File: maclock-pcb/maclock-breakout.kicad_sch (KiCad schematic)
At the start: 10 parts, among them SW1 SW_Push, SW2 SW_Push

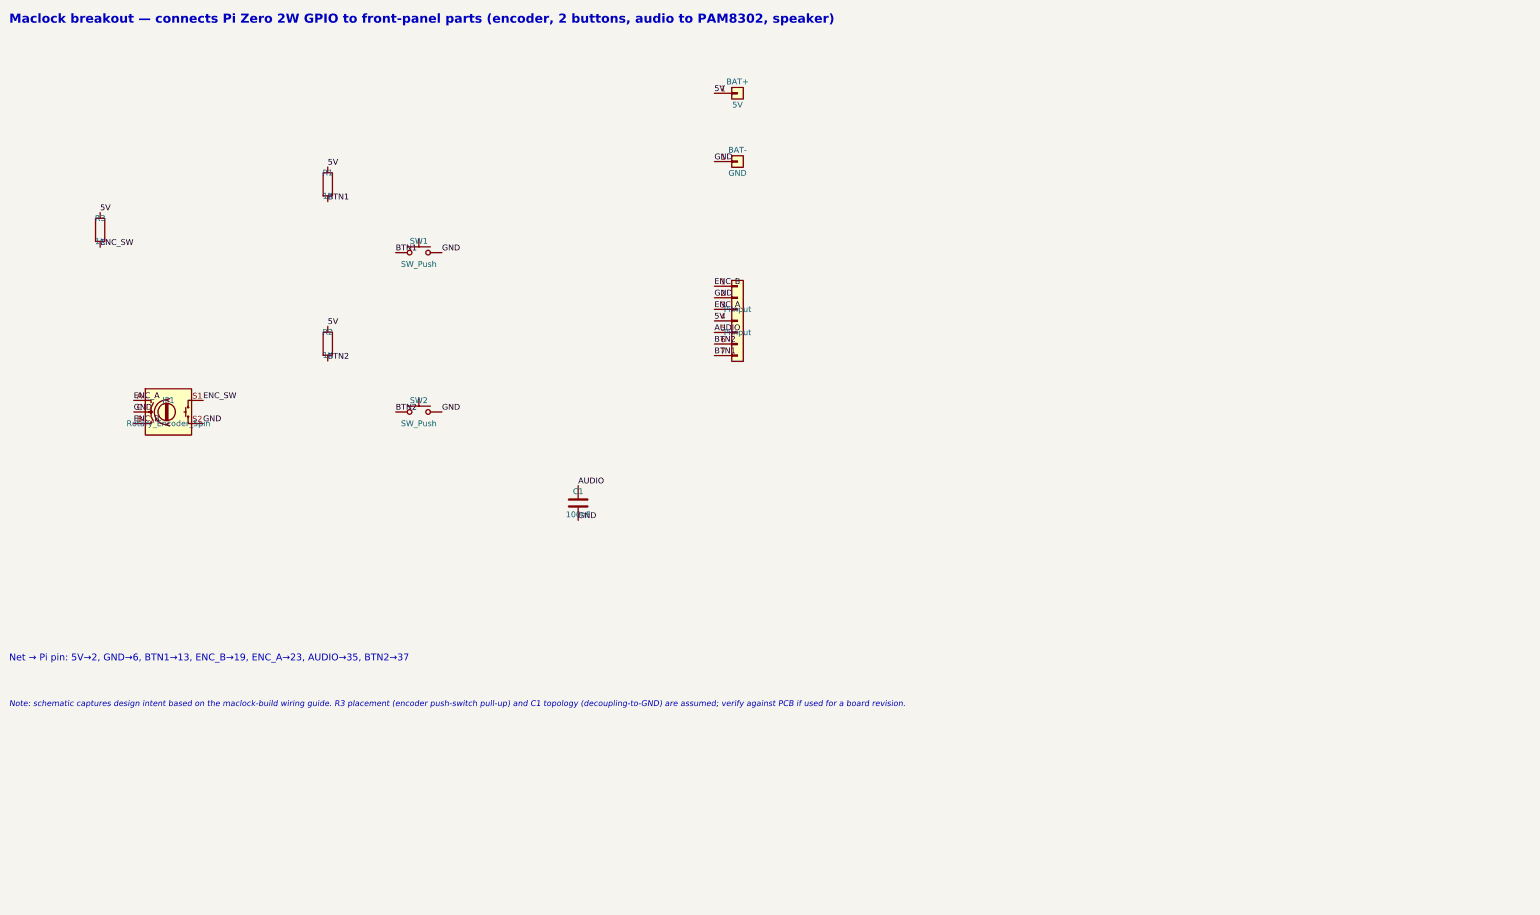
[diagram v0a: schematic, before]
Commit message: PCB: real HYCW03 encoder, LCSC-sourceable BOM, rebuilt schematic
- ENC1: F-Switch E8E8-3.2C60-9B34 (not on LCSC) -> HOAUC HYCW03-2.8D-5P-S
  (C55218995); new footprint, bore placed 8.8mm from the left edge / 4mm from
  the bottom to keep the dial aligned with the case
- Nets: split the series-resistor button nets (BTN1/SW1, BTN2/SW2) so each is
  fully connected; assigned ENC1 pad nets; normalized all board nets to the
  /-prefixed hierarchical form to match the schematic
- Rebuilt maclock-breakout.kicad_sch from the PCB (was a PiInput-only stub):
  all 11 parts with correct footprints/values/LCSC, custom ENC1 symbol in
  maclock.kicad_sym; ERC 0/0, board<->schematic parity clean but for benign
  symbol metadata
- BOM: every part now resolves to an LCSC number (added J1 C158011, J2 C157997);
  PCBWAY_REPLY.md answers the quote's four flagged parts
- Switches: added TS24CA and TSB001 side-switch footprints as LCSC-stocked
  alternatives to the Same Sky TS32; board left on the TS32 for hand-positioning
- scripts/: reproducible pcbnew edits (bundled Python) for each board change
- README: BOM, sourcing, J1 power switch / J2 power input, schematic status
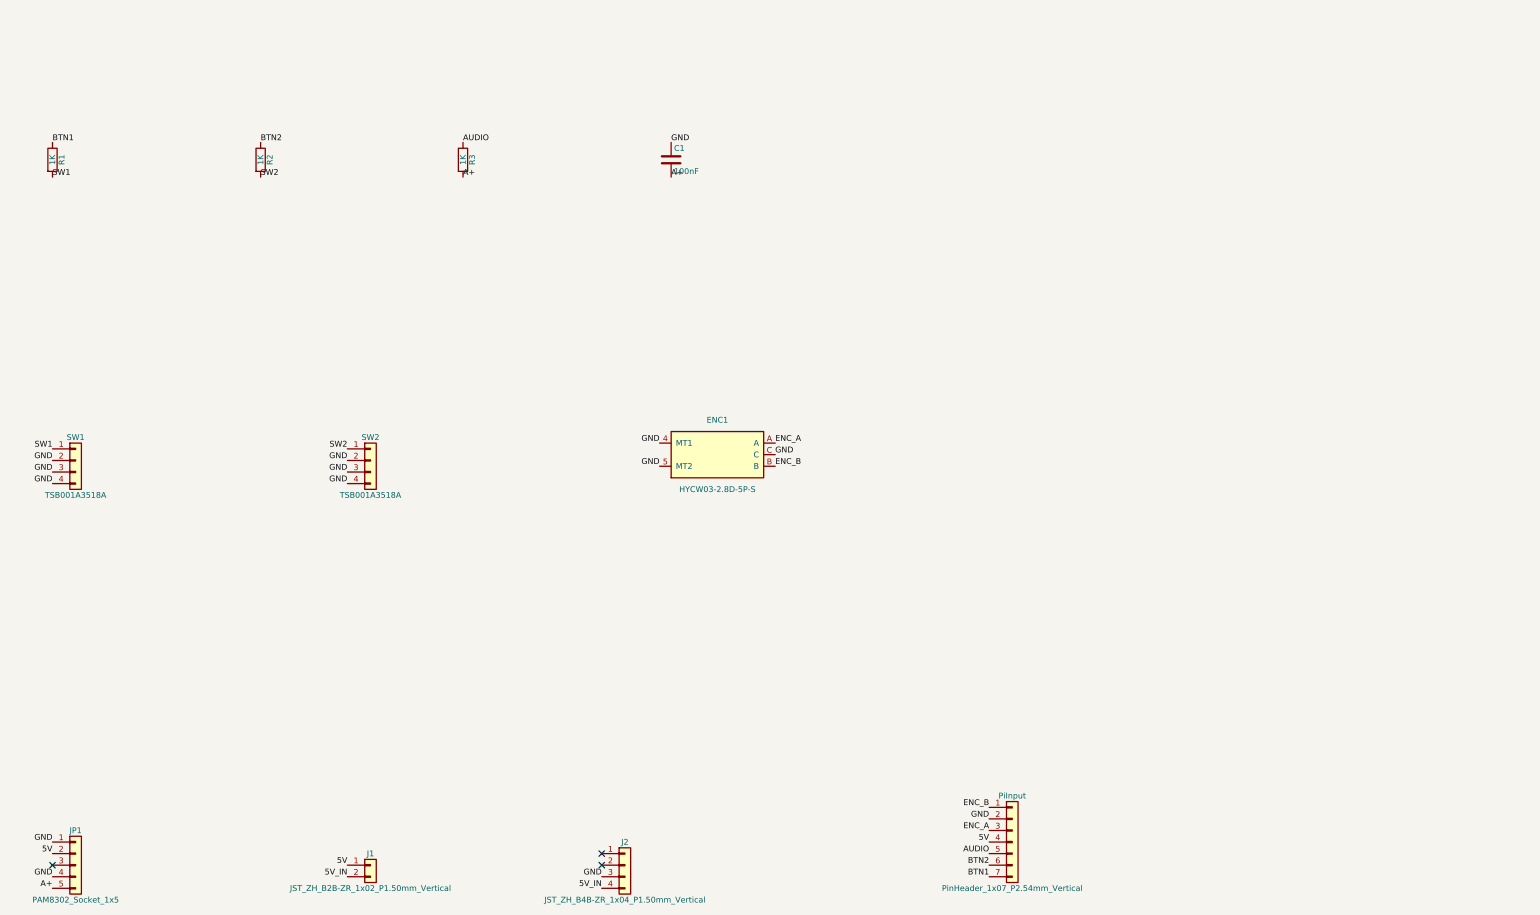
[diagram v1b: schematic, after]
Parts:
- removed BAT+: 5V, symbol Connector_Generic:Conn_01x01
- removed BAT-: GND, symbol Connector_Generic:Conn_01x01
- removed JP1: Rotary_Encoder_5pin, KiCad:1X05_ROUND_70, symbol Device:RotaryEncoder_Switch
- removed SW1, SW2: SW_Push, KiCad:TS32735BK160RASMTTR, symbol Switch:SW_Push
- added ENC1: HYCW03-2.8D-5P-S, maclock:RotaryEncoder_HYCW03-2.8D-5P-S_SMD, symbol maclock:RotaryEncoder_HYCW03-2.8D-5P-S
- added J1: JST_ZH_B2B-ZR_1x02_P1.50mm_Vertical, Connector_JST:JST_ZH_B2B-ZR_1x02_P1.50mm_Vertical, symbol Connector_Generic:Conn_01x02
- added J2: JST_ZH_B4B-ZR_1x04_P1.50mm_Vertical, Connector_JST:JST_ZH_B4B-ZR_1x04_P1.50mm_Vertical, symbol Connector_Generic:Conn_01x04
- added JP1: PAM8302_Socket_1x5, Connector_PinSocket_2.54mm:PinSocket_1x05_P2.54mm_Vertical, symbol Connector_Generic:Conn_01x05
- added SW1, SW2: TSB001A3518A, maclock:SW_TSB001_7.7x3.55_SideSMD, symbol Connector_Generic:Conn_01x04
- C1: footprint Capacitor_THT:C_Disc_D6.0mm_W2.5mm_P5.00mm -> maclock:C_Chip_or_Disc_P5mm_SMD; LCSC (none) -> C24497
- PiInput: value PiInput -> PinHeader_1x07_P2.54mm_Vertical; LCSC (none) -> C492406
- R1, R2, R3: LCSC (none) -> C11702
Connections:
- net 5V: now also J1.1 (Pin_1), JP1.2 (Pin_2); no longer R1.1, R2.1, R3.1
- net AUDIO: now also R3.1; no longer C1.1
- net BTN1: now also R1.1; no longer R1.2
- net BTN2: now also R2.1; no longer R2.2
- net ENC_A: now also ENC1.A
- net ENC_B: now also ENC1.B
- net GND: now also C1.1, ENC1.4 (MT1), ENC1.5 (MT2), ENC1.C, J2.3 (Pin_3), JP1.1 (Pin_1), JP1.4 (Pin_4), SW1.2 (Pin_2), SW1.3 (Pin_3), SW1.4 (Pin_4), SW2.2 (Pin_2), SW2.3 (Pin_3), SW2.4 (Pin_4); no longer C1.2
- net ENC_SW renamed A+
- net A+: now also C1.2, JP1.5 (Pin_5)
- new net 5V_IN: J1.2 (Pin_2), J2.4 (Pin_4)
- new net SW1: R1.2, SW1.1 (Pin_1)
- new net SW2: R2.2, SW2.1 (Pin_1)
- no-connect marks 0 -> 3
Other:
- note removed: "Maclock breakout — connects Pi Zero 2W GPIO to front-panel parts (encoder, 2 buttons, audio to PAM8302, speaker)"
- note removed: "Net → Pi pin: 5V→2, GND→6, BTN1→13, ENC_B→19, ENC_A→23, AUDIO→35, BTN2→37"
- note removed: "Note: schematic captures design intent based on the maclock-build wiring guide. R3 placement (encoder push-switch pull-up) and C1 topology (decoupling-to-GND) are assumed; verify against PCB if used for a board revision."

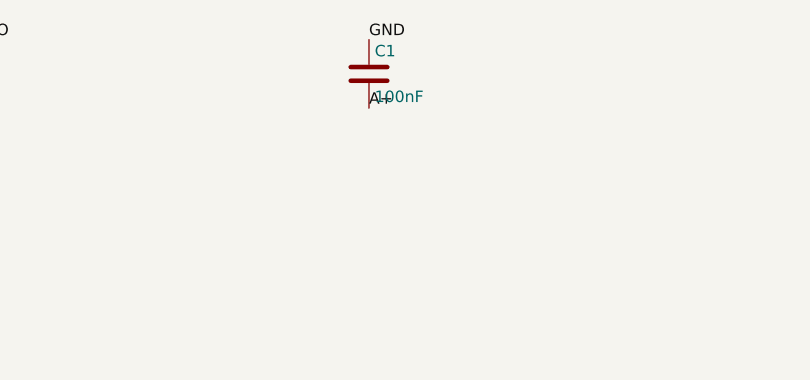
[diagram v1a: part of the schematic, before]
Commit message: PCB: TSB001 part numbers on board, C1 10nF audio LPF, J2 polarity silk, project lib tables, C1 1206 model
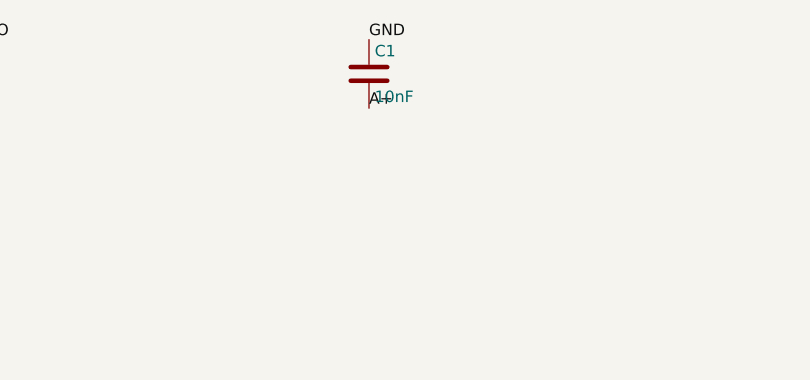
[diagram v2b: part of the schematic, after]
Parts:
- C1: value 100nF -> 10nF; LCSC C24497 -> C1846
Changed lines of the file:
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@@
 			)
 		)
-		(property "Value" "100nF"
+		(property "Value" "10nF"
 			(at 186.055 57.15 0)
 			(effects
@@
 			)
 		)
-		(property "LCSC" "C24497"
+		(property "LCSC" "C1846"
 			(at 185.42 54.61 0)
 			(hide yes)

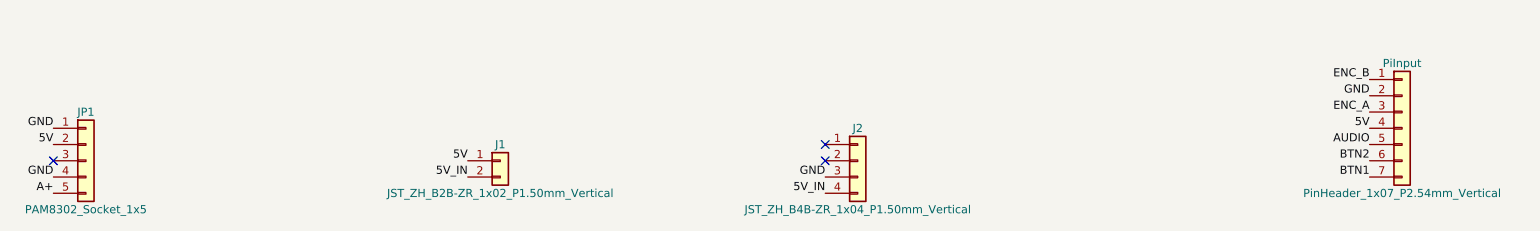
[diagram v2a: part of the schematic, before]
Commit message: PCB: connector MPN values, 1.0 mm 5V supply tracks
- J1/J2/JP1/PiInput Value -> B2B-ZR(LF)(SN) / B4B-ZR(LF)(SN) / 2.54-1*5PFemale / PZ254V-11-07P
  on board and schematic (PCBway reads the board's Value column)
- /5V and /5V_IN tracks 0.5 -> 1.0 mm; the J2 pad-1 skirt is 0.8 mm and the diagonal out of
  JP1 pin 2 stays 0.5 mm (2.54 mm socket pitch); long y=98 run restarted at x=141 with a stub
  so its round end clears JP1 pin 1 (GND)
- DRC 0 errors / 0 unconnected; ERC 0; scripts/mpn_values_and_wide_5v.py
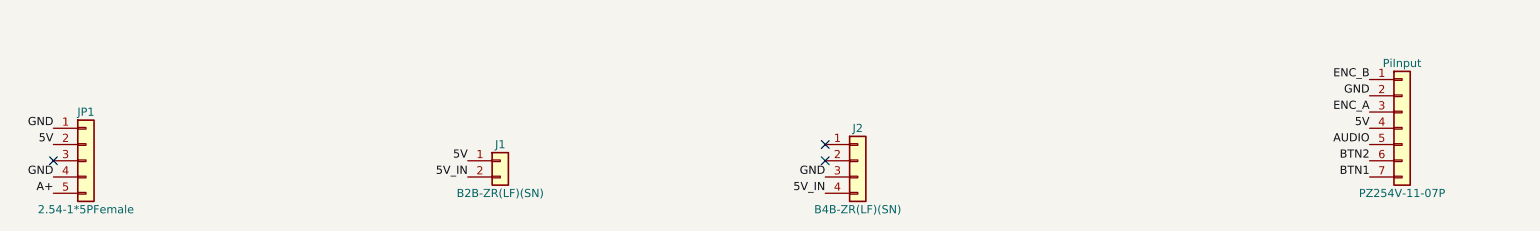
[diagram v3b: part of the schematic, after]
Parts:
- J1: value JST_ZH_B2B-ZR_1x02_P1.50mm_Vertical -> B2B-ZR(LF)(SN)
- J2: value JST_ZH_B4B-ZR_1x04_P1.50mm_Vertical -> B4B-ZR(LF)(SN)
- JP1: value PAM8302_Socket_1x5 -> 2.54-1*5PFemale
- PiInput: value PinHeader_1x07_P2.54mm_Vertical -> PZ254V-11-07P
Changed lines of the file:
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@@
 			)
 		)
-		(property "Value" "PAM8302_Socket_1x5"
+		(property "Value" "2.54-1*5PFemale"
 			(at 54.61 217.17 0)
 			(effects
@@
 			)
 		)
-		(property "Value" "JST_ZH_B2B-ZR_1x02_P1.50mm_Vertical"
+		(property "Value" "B2B-ZR(LF)(SN)"
 			(at 119.38 214.63 0)
 			(effects
@@
 			)
 		)
-		(property "Value" "JST_ZH_B4B-ZR_1x04_P1.50mm_Vertical"
+		(property "Value" "B4B-ZR(LF)(SN)"
 			(at 175.26 217.17 0)
 			(effects
@@
 			)
 		)
-		(property "Value" "PinHeader_1x07_P2.54mm_Vertical"
+		(property "Value" "PZ254V-11-07P"
 			(at 260.35 214.63 0)
 			(effects

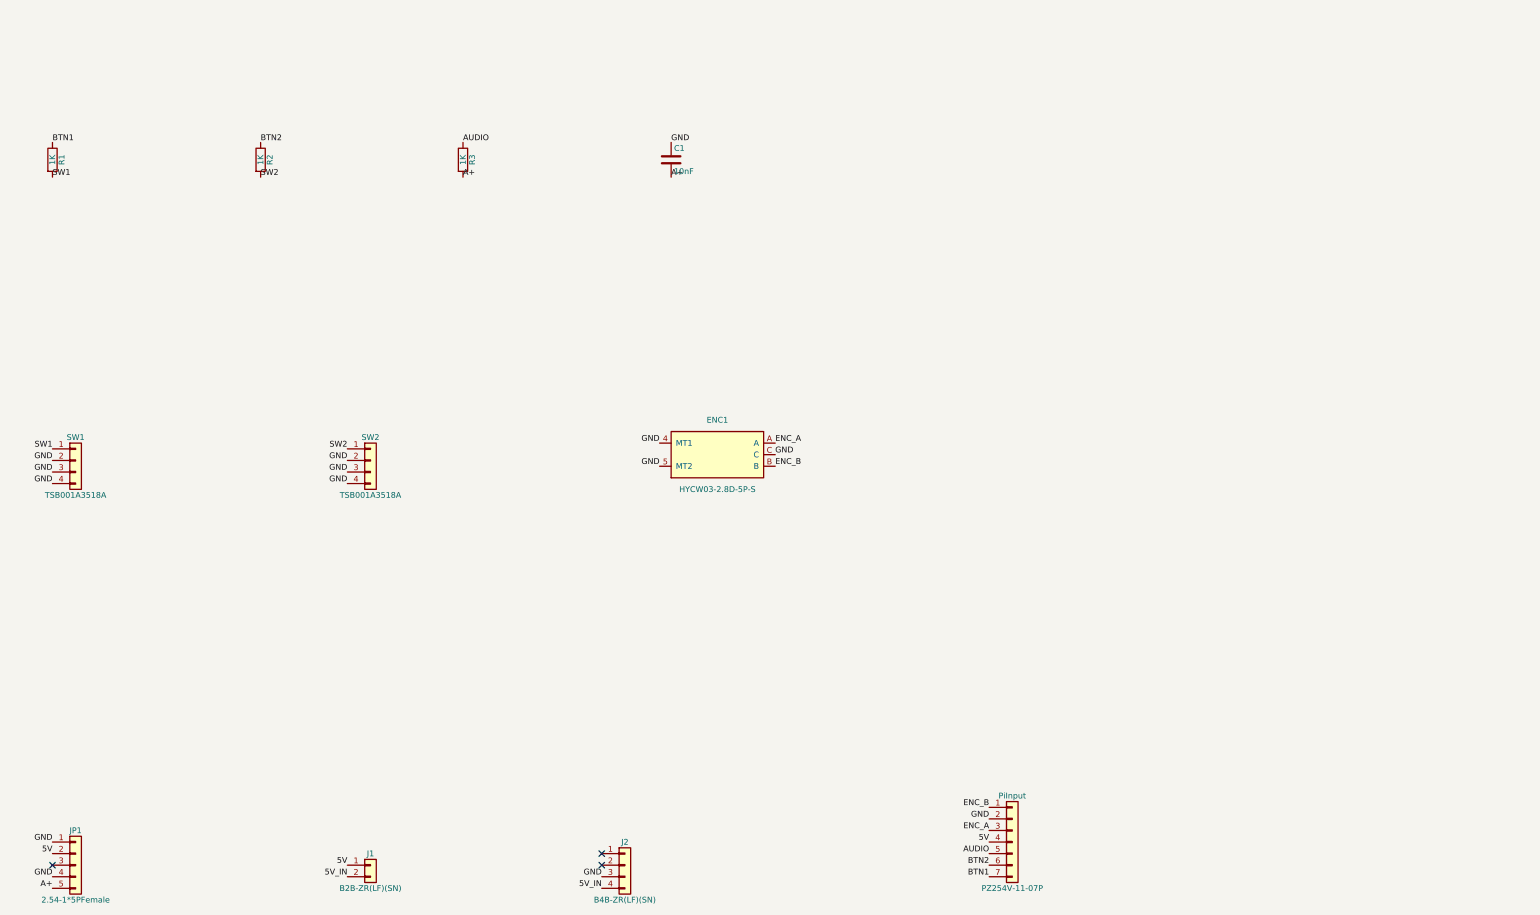
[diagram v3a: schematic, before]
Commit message: PCB rev 2: on-board PAM8302A amp replaces the Adafruit module
- U1 PAM8302AASCR (C113367) on the bottom side where the JP1 socket was; JP1 removed
- Input: A+ -> C2 220n -> R4 47k -> IN+; IN- via R5 47k + C3 220n to GND (gain ~9 dB)
- C4 1u + C5 10u decoupling, fed by via from the F.Cu 5V trunk; new 5V via at the old
  JP1 pin-2 spot keeps the F.Cu/B.Cu 5V runs joined
- SD pulled up by R6 100k; also brought out on a new PiInput pin 8 (MUTE) along the
  top edge, so the header is now 1x8 (C492407)
- J3 JST ZH 2P speaker connector (C158011), + / - silk, pad 1 = SPK+
- Schematic: new parts + nets, PWR_FLAGs on 5V/GND; ERC 0/0. DRC 0 errors, 0 unconnected,
  parity only benign field/NC notes. scripts/add_onboard_amp.py rebuilds it from 5ece6d9
- Docs: PCB README BOM + amp section, PCBway reply, build-guide wiring table, root README
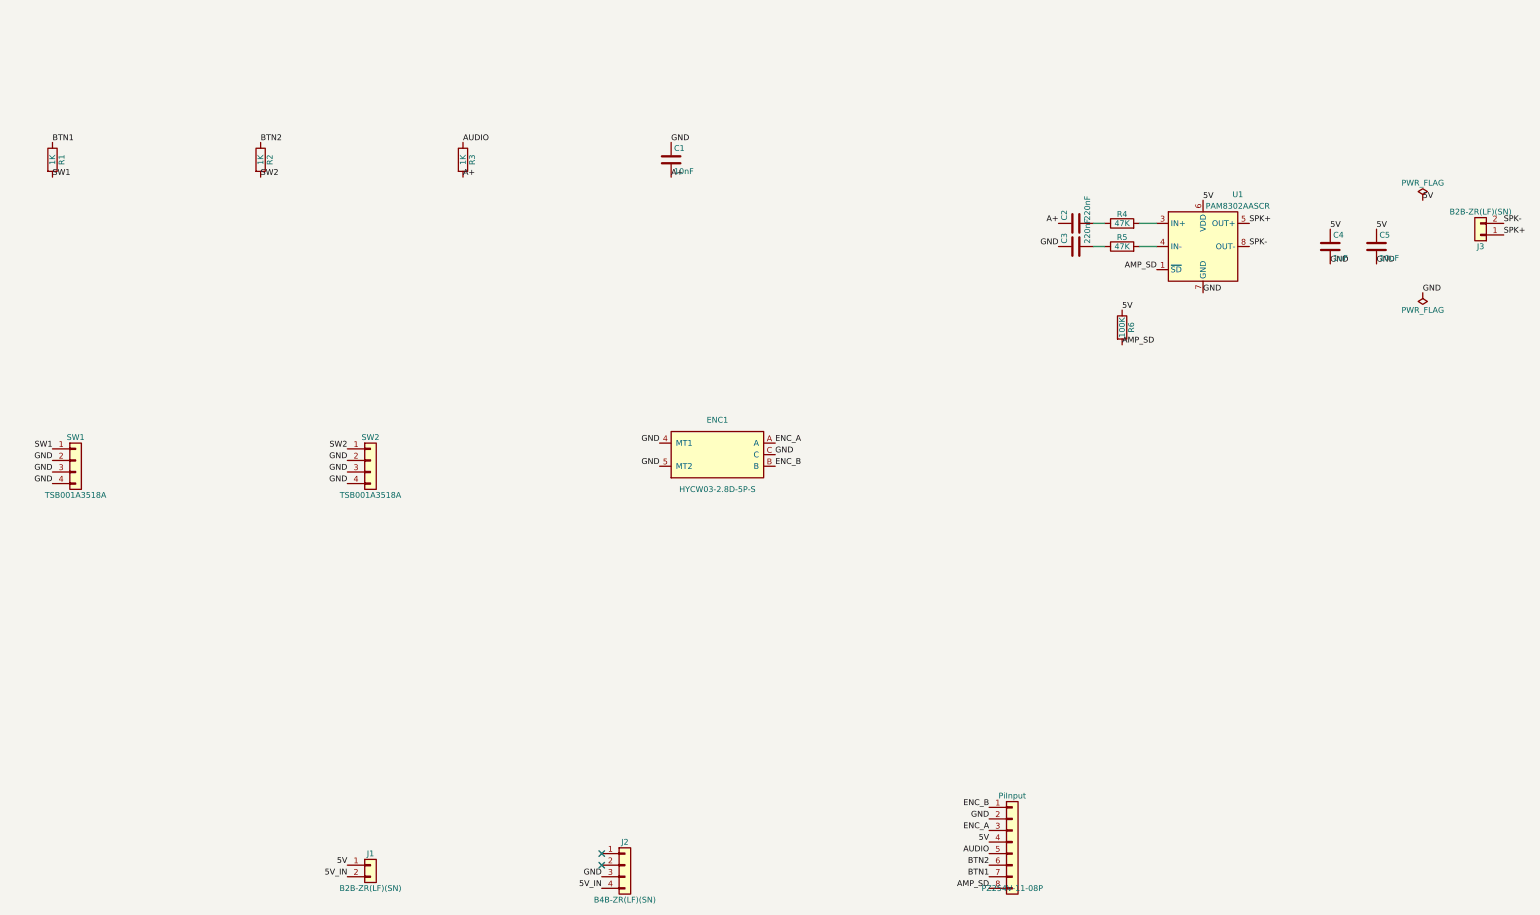
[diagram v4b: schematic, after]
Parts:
- removed JP1: 2.54-1*5PFemale, Connector_PinSocket_2.54mm:PinSocket_1x05_P2.54mm_Vertical, symbol Connector_Generic:Conn_01x05
- added C2, C3: 220nF, Capacitor_SMD:C_0603_1608Metric, symbol Device:C
- added C4: 1uF, Capacitor_SMD:C_0603_1608Metric, symbol Device:C
- added C5: 10uF, Capacitor_SMD:C_0805_2012Metric, symbol Device:C
- added J3: B2B-ZR(LF)(SN), Connector_JST:JST_ZH_B2B-ZR_1x02_P1.50mm_Vertical, symbol Connector_Generic:Conn_01x02
- added R4, R5: 47K, Resistor_SMD:R_0402_1005Metric_Pad0.72x0.64mm_HandSolder, symbol Device:R
- added R6: 100K, Resistor_SMD:R_0402_1005Metric_Pad0.72x0.64mm_HandSolder, symbol Device:R
- added U1: PAM8302AASCR, Package_SO:MSOP-8_3x3mm_P0.65mm, symbol Amplifier_Audio:PAM8302AAS
- PiInput: value PZ254V-11-07P -> PZ254V-11-08P; footprint Connector_PinHeader_2.54mm:PinHeader_1x07_P2.54mm_Vertical -> Connector_PinHeader_2.54mm:PinHeader_1x08_P2.54mm_Vertical; symbol Connector_Generic:Conn_01x07 -> Connector_Generic:Conn_01x08; LCSC C492406 -> C492407
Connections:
- net 5V: now also C4.1, C5.1, R6.1, U1.6 (VDD)
- net A+: now also C2.1
- net GND: now also C3.1, C4.2, C5.2, U1.7 (GND)
- new net: C2.2, R4.1
- new net: R4.2, U1.3 (IN+)
- new net: R5.2, U1.4 (IN-)
- new net: C3.2, R5.1
- new net AMP_SD: PiInput.8 (Pin_8), R6.2, U1.1 (~{SD})
- new net SPK+: J3.1 (Pin_1), U1.5 (OUT+)
- new net SPK-: J3.2 (Pin_2), U1.8 (OUT-)
- no-connect marks 3 -> 2

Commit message: C1: plain 0603 land (10nF X7R, C57112) replaces the chip-or-disc hybrid
- All passives are SMD now; the hybrid THT/SMD land and its library footprint are gone
- C1 sits vertically at (143.925, 92.96) on B.Cu, A+ on top toward R3, GND below to the pour
- scripts/c1_plain_0603.py replays it from 5d96fa9; ERC 0, DRC 0 errors / 0 unconnected
- README BOM, sourcing table and PCBway reply updated; the 'chip or disc' section removed
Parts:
- C1: footprint maclock:C_Chip_or_Disc_P5mm_SMD -> Capacitor_SMD:C_0603_1608Metric; LCSC C1846 -> C57112
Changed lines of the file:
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@@
 			)
 		)
-		(property "Footprint" "maclock:C_Chip_or_Disc_P5mm_SMD"
+		(property "Footprint" "Capacitor_SMD:C_0603_1608Metric"
 			(at 185.42 54.61 0)
 			(hide yes)
@@
 			)
 		)
-		(property "LCSC" "C1846"
+		(property "LCSC" "C57112"
 			(at 185.42 54.61 0)
 			(hide yes)
